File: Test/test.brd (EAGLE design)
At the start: 63.5 x 24.1 mm, 47 parts, among them J2 1755529, U1 STM32F405RGT6, U2 CSD88584Q5DCT, U3 CSD88584Q5DCT, U4 CSD88584Q5DCT, Y1 ECS-80-S-4X

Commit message: couple improvements to the board and datasheets
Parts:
- added J1: 284512-3, ThrusterConnector:284512-3
- added U$1: MURATA-DC-DC, MURATA_3pin_dcdc:MURATA-DC-DC
- C11: value 4.7uF -> 20[F
- C2: value 4.7uF -> 20pF
- R3, R5: value 1k -> 0
- RESET1: device DiscreteComponents:SW_2512 -> Push button - FSM2JMTR:DISCRETECOMPONENTS_SW_2512
- moved R4 18.9 mm to (56.8, 23.9), flipped to the top, turned to 270 degrees
- moved R29 10.6 mm to (52.0, 17.5), turned to 90 degrees
- moved Y1 7.64 mm to (45.0, 23.2)
- moved C2 5.48 mm to (49.4, 22.8)
- moved C10 5.06 mm to (38.4, 22.4), turned to 180 degrees
- moved R3 4.31 mm to (42.2, 21.0)
- moved RESET1 3.89 mm to (36.8, 24.6)
- moved R5 3.82 mm to (42.7, 19.3)
- moved C31 3.02 mm to (53.5, 19.3), turned to 270 degrees
- moved C11 2.70 mm to (44.6, 23.7), turned to 90 degrees
- moved R28 2.61 mm to (55.1, 17.6), turned to 270 degrees
- moved C14 2.08 mm to (30.5, 4.42), turned to 180 degrees
- moved C30 1.40 mm to (53.6, 13.0), turned to 90 degrees
- moved R11 0.77 mm to (26.4, 3.53), flipped to the bottom
- moved R10 0.71 mm to (24.0, 3.89), turned to 180 degrees
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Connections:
- net 12V: now also U$1.1
- net 3V3: now also SV1.8, U$1.3; no longer SV1.6
- net CAN_H: now also SV1.3; no longer SV1.5
- net CAN_L: now also SV1.2; no longer SV1.4
- net GND: now also SV1.6, U$1.2; no longer SV1.7
- net NRST: now also SV1.4; no longer SV1.8
- net PHASE_A1: now also J1.3
- net PHASE_B1: now also J1.2
- net PHASE_C1: now also J1.1
- net SWCLK: now also SV1.7; no longer SV1.3
- net SWDIO: now also SV1.5; no longer SV1.2
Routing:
- net NRST: track 31.6 -> 46.8 mm
- net 3V3: track 69.6 -> 56.9 mm, vias 7 -> 1
- net 12V: track 46.8 -> 59.2 mm
- net CAN_L: track 8.94 -> 16.8 mm
- net N$46: track 10.5 -> 3.15 mm
- net SWCLK: track 16.5 -> 23.1 mm, vias 0 -> 1
- net SWDIO: track 22.4 -> 27.7 mm, vias 0 -> 1
- net EN_1: track 15.4 -> 10.2 mm, vias 2 -> 1
- net CAN_H: track 9.10 -> 12.8 mm
- net OSC_IN: track 5.66 -> 3.05 mm
- net OSC_OUT: track 7.03 -> 4.77 mm
- net N$19: track 4.98 -> 3.45 mm
- net GND: track 5.23 -> 6.63 mm
- net DVDD_1: track 12.9 -> 11.6 mm, vias 2 -> 1
- net GLB_1: track 13.2 -> 14.4 mm
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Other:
- board size 63.5 x 24.1 mm -> 65.8 x 27.6 mm

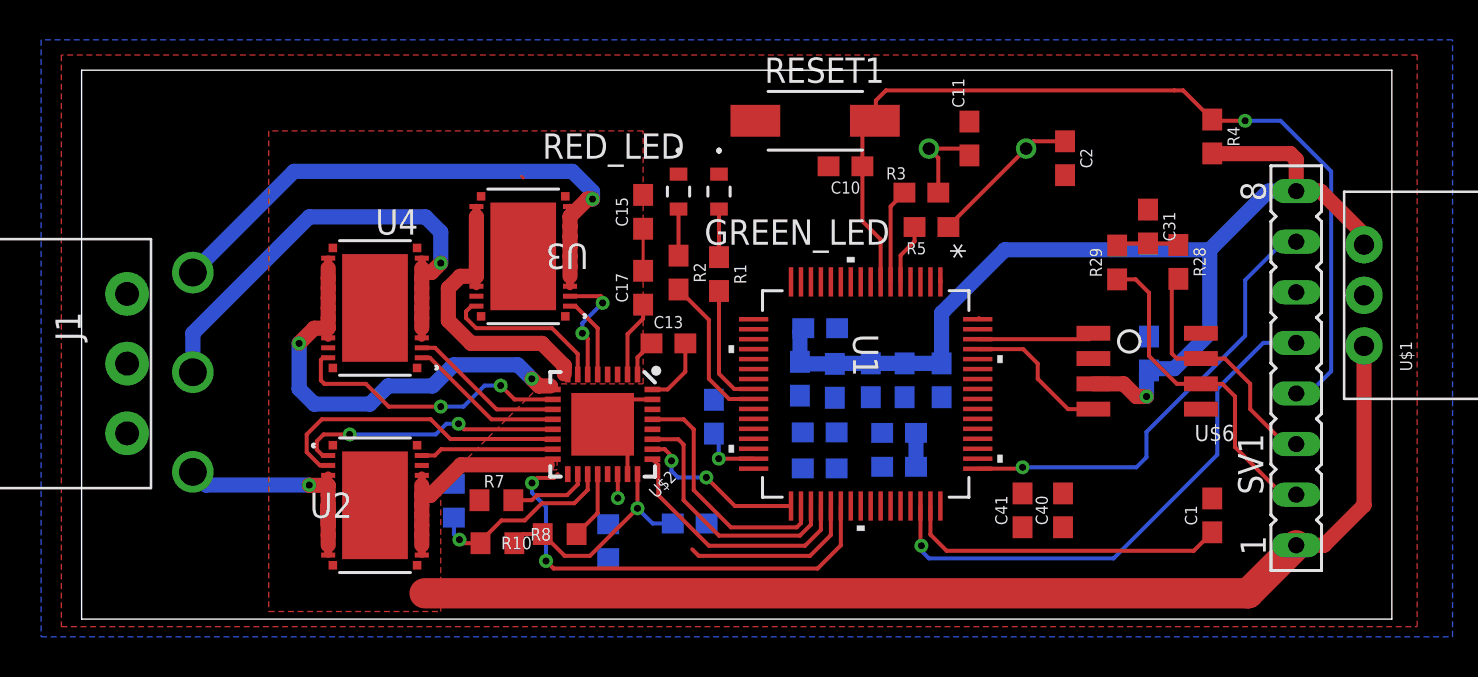
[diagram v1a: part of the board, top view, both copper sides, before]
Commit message: grounded drain of low side fets and other improvements
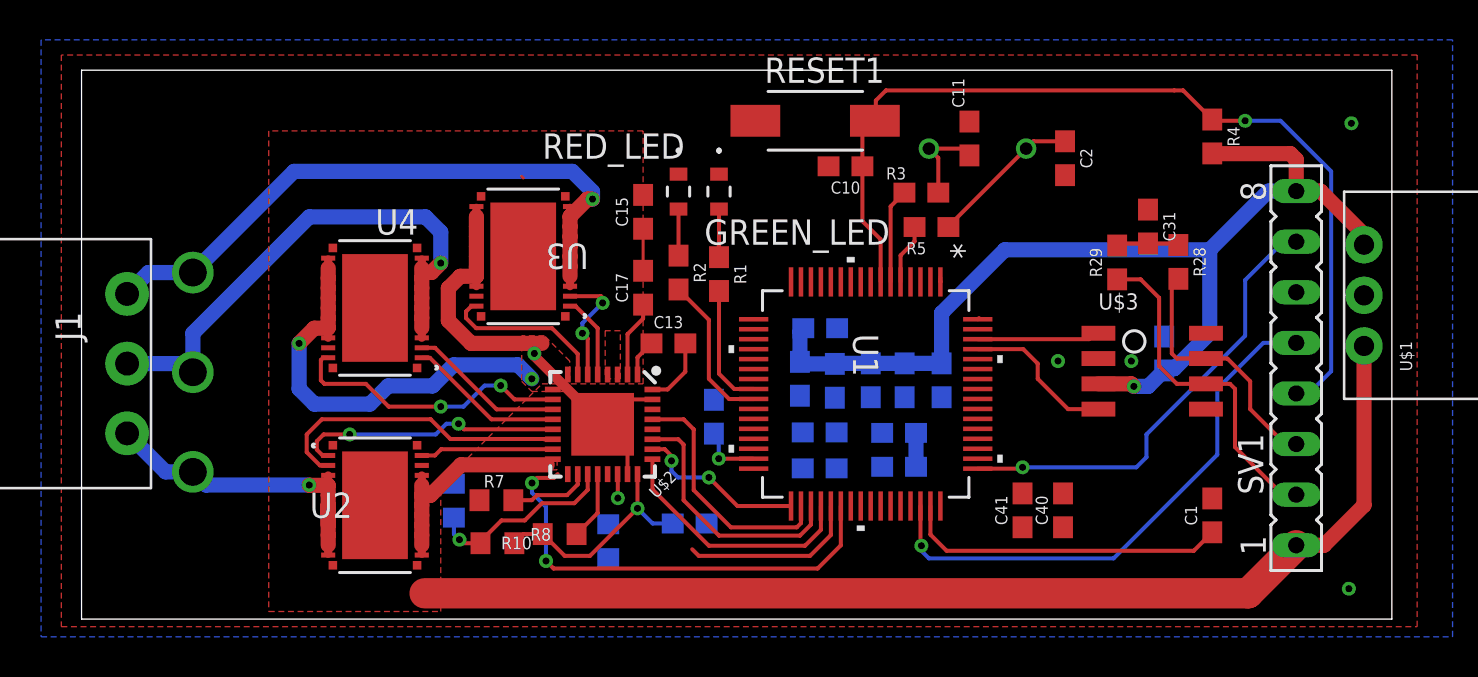
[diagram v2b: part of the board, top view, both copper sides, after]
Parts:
- removed U$6: TCAN337D, PI_Shield_Library:TCAN337D
- added U$3: TCAN337D, STM and CAN parts:SOIC-8
- C10: value 4.7uF -> 0.1uF
- C30: value 4.7uF -> 0.1IuF
- R1, R2: value 1k -> 470
- R4: value 1k -> 10k
- moved C30 0.76 mm to (54.4, 13.0)
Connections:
- net N$1 renamed LED1
- net N$2 renamed LED1_MID
- net N$3 renamed LED2_MID
- net N$4 renamed LED2
- removed net INL_1: U$2.26, U$2.28, U$2.30, U1.33
- removed net SLA_1: U$2.8, U3.12, U3.13, U3.14, U3.15, U3.16, U3.17, U3.18, U3.19, U3.20
- removed net SLB_1: U$2.9, U4.12, U4.13, U4.14, U4.15, U4.16, U4.17, U4.18, U4.19, U4.20
- removed net SLC_1: U$2.16, U2.12, U2.13, U2.14, U2.15, U2.16, U2.17, U2.18, U2.19, U2.20
- new net INLA_1: U$2.26, U1.33
- new net INLB_1: U$2.28
- new net INLC_1: U$2.30
- net 3V3: now also U$3.3; no longer U$6.VCC
- net CAN_H: now also U$3.7; no longer U$6.CANH
- net CAN_L: now also U$3.6; no longer U$6.CANL
- net CAN_RX: now also U$3.4; no longer U$6.RXD
- net CAN_TX: now also U$3.1; no longer U$6.TXD
- net GND: now also U$2.16, U$2.8, U$2.9, U$3.2, U2.12, U2.13, U2.14, U2.15, U2.16, U2.17, U2.18, U2.19, U2.20, U3.12, U3.13, U3.14, U3.15, U3.16, U3.17, U3.18, U3.19, U3.20, U4.12, U4.13, U4.14, U4.15, U4.16, U4.17, U4.18, U4.19, U4.20; no longer U$6.GND
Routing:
- net GND: track 6.63 -> 57.1 mm, vias 0 -> 7
- net SLB_1: track 22.2 -> 0.00 mm, vias 2 -> 0
- net SLA_1: track 15.5 -> 0.00 mm
- net SLC_1: track 10.9 -> 0.00 mm
- net INL_1: track 8.58 -> 0.00 mm, vias 2 -> 0
- net INLA_1: track 0.00 -> 8.58 mm, vias 0 -> 2
- net PHASE_C1: track 12.5 -> 16.6 mm
- net PHASE_A1: track 28.4 -> 32.1 mm
- net PHASE_B1: track 23.3 -> 26.8 mm
- net 3V3: track 56.9 -> 55.5 mm
- removed copper zone on layer 1, net SLA_1
- removed copper zone on layer 1, net SLB_1
- removed copper zone on layer 1, net SLC_1

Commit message: progress
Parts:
- removed GREEN_LED, RED_LED: TLMS1100-GS08, VESC_SHIT:LED_VISHAY_TLMX1100
- removed J2: 1755529, VESC_SHIT:CONN_1755529
- removed U2, U3, U4: CSD88584Q5DCT, VESC_SHIT:DMM0022A
- added D1: RED, LED-0805:0805
- added D2: GREEN, LED-0805:0805
- added JP2, JP4, JP6: JUMPER-SMT_2_NC_TRACE_SILK, SparkFun-Jumpers:SMT-JUMPER_2_NC_TRACE_SILK
- added Q1, Q2, Q3: (no value), Dual NMOS:SO08
- added U$4: 3PINCONNECTOR, afro_20A_esc:3PINCONNECTOR
- C11: value 20[F -> 20pF
- U$2: device VESC_SHIT:QFN-32-5X5MM -> Motor Driver - DRV8320HRTVT:QFN-32-5X5MM
- U1: value STM32F405RGT6 -> (none); device VESC_SHIT:LQFP-64 -> STM32F405RGT6:LQFP-64
- moved C10 1.02 mm to (38.4, 21.3)
- moved R11 0.51 mm to (25.9, 3.53)
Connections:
- net DVDD_1 renamed 3V3_OUT
- net N$16 renamed CPL
- net N$17 renamed IDRIVE
- net N$18 renamed MODE
- net N$34 renamed V_CAP_L
- net N$9 renamed CPH
- removed net SHA_1: U$2.6, U3.2
- removed net SHB_1: U$2.11, U4.2
- removed net SHC_1: U$2.14, U2.2
- new net DLA_1: JP2.1
- new net DLB_1: JP4.1
- new net DLC_1: JP6.1
- net 12V: now also Q1.5, Q1.6, Q2.7, Q2.8, Q3.7, Q3.8; no longer U2.27, U3.27, U4.27
- net GHA_1: now also Q1.4; no longer U3.1
- net GHB_1: now also Q2.2; no longer U4.1
- net GHC_1: now also Q3.2; no longer U2.1
- net GLA_1: now also Q1.2; no longer U3.22
- net GLB_1: now also Q2.4; no longer U4.22
- net GLC_1: now also Q3.4; no longer U2.22
- net GND: now also D1.C, D2.C, Q1.1, Q2.3, Q3.3; no longer GREEN_LED.1, RED_LED.1, U2.12, U2.13, U2.14, U2.15, U2.16, U2.17, U2.18, U2.19, U2.20, U3.12, U3.13, U3.14, U3.15, U3.16, U3.17, U3.18, U3.19, U3.20, U4.12, U4.13, U4.14, U4.15, U4.16, U4.17, U4.18, U4.19, U4.20
- net LED1_MID: now also D1.A; no longer GREEN_LED.2
- net LED2_MID: now also D2.A; no longer RED_LED.2
- net PHASE_A1: now also JP2.2, Q1.3, Q1.7, Q1.8, U$2.6, U$4.A; no longer J2.1, U3.10, U3.11, U3.3, U3.4, U3.5, U3.6, U3.7, U3.8, U3.9
- net PHASE_B1: now also JP4.2, Q2.1, Q2.5, Q2.6, U$2.11, U$4.B; no longer J2.2, U4.10, U4.11, U4.3, U4.4, U4.5, U4.6, U4.7, U4.8, U4.9
- net PHASE_C1: now also JP6.2, Q3.1, Q3.5, Q3.6, U$2.14, U$4.C; no longer J2.3, U2.10, U2.11, U2.3, U2.4, U2.5, U2.6, U2.7, U2.8, U2.9
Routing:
- net GND: track 57.1 -> 14.7 mm, vias 7 -> 35
- net SHC_1: track 15.3 -> 0.00 mm
- net GHA_1: track 4.17 -> 15.8 mm
- net PHASE_C1: track 16.6 -> 25.7 mm, vias 1 -> 0
- net SHB_1: track 7.86 -> 0.00 mm
- net SHA_1: track 6.05 -> 0.00 mm, vias 2 -> 0
- net GHC_1: track 13.4 -> 7.77 mm, vias 2 -> 0
- net EN_1: track 10.2 -> 15.4 mm, vias 1 -> 2
- net GLB_1: track 14.4 -> 9.90 mm, vias 2 -> 0
- net 3V3: track 55.5 -> 51.5 mm
- net GLA_1: track 8.35 -> 12.3 mm
- net 12V: track 59.2 -> 62.7 mm, vias 0 -> 22
- net SWDIO: track 27.7 -> 30.8 mm
- net PHASE_A1: track 32.1 -> 35.2 mm, vias 1 -> 0
- net LED1_MID: track 2.41 -> 0.00 mm
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- added copper zone on layer 16, net 12V
